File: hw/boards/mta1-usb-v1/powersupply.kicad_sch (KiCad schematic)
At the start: 19 parts, among them U1 MCP1824T-2502EOT, U2 MIC5258-1.2YM5, U9 NCP752BSN33T1G

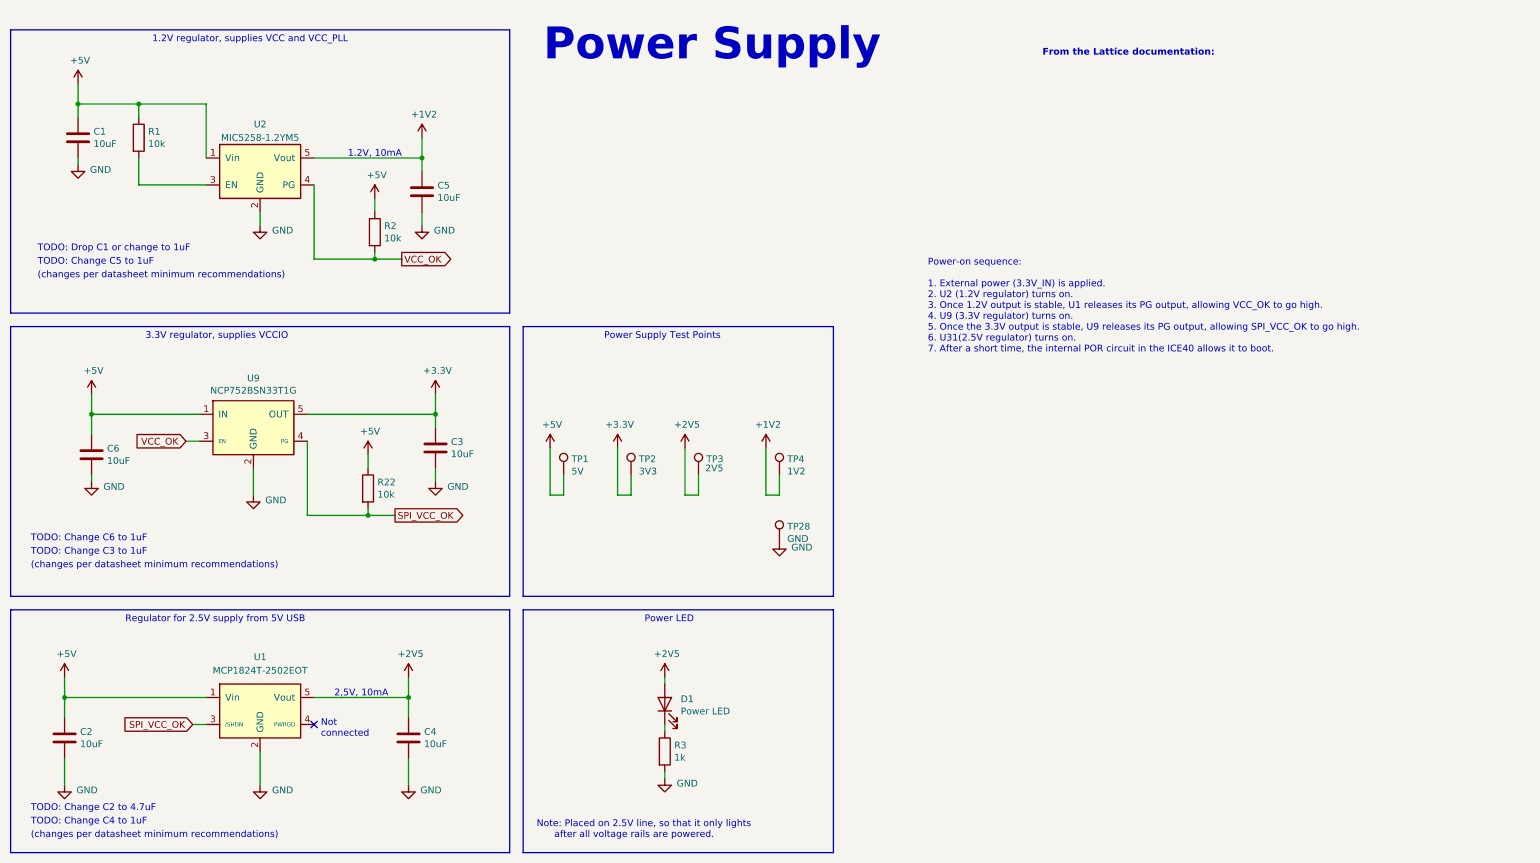
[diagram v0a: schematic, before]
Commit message: Add extended values, manufacturer/distributor info to components in mta1
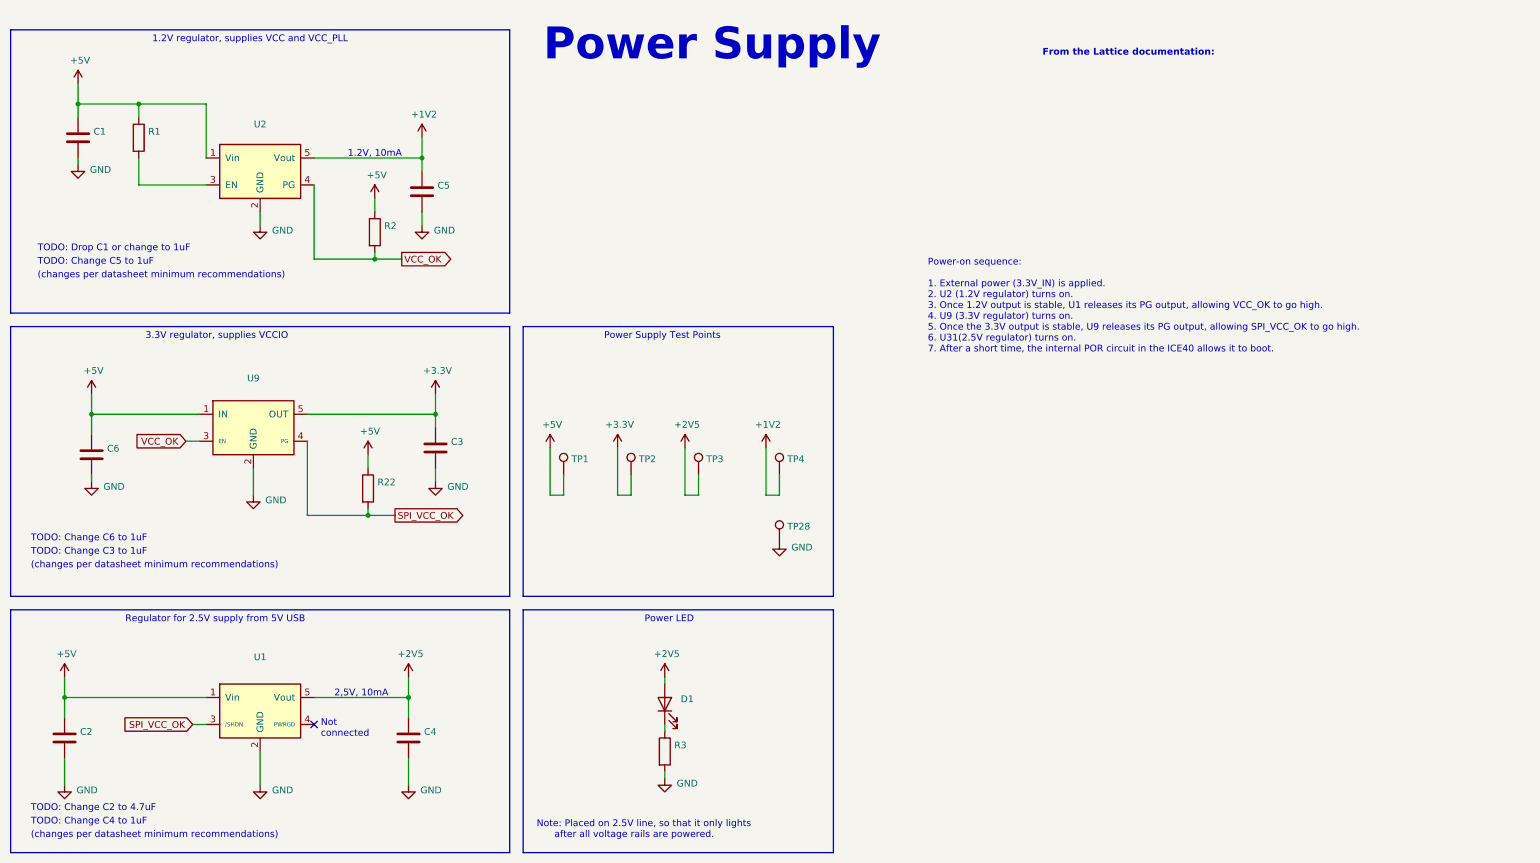
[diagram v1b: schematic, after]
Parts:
- C1, C2, C3, C4, C5, C6: value 10uF -> (none); footprint mta1:CAPC1608X09L -> (none); Extended Value (none) -> 10V,X5R,20%; Manufacturer (none) -> Any/not critical
- D1: value Power LED -> (none); footprint LED_SMD:LED_0402_1005Metric -> (none); Manufacturer (none) -> Foshan NationStar; Manufacturer Part Number (none) -> NCD0402B1; Supplier (none) -> LCSC; Supplier Part Number (none) -> C130724
- R1, R2, R22: value 10k -> (none); footprint mta1:ERJ2G(0402)_L -> (none); Extended Value (none) -> 1/16W,5%; Manufacturer (none) -> Any/not critical
- R3: value 1k -> (none); footprint mta1:ERJ2G(0402)_L -> (none); Extended Value (none) -> 1/16W,5%; Manufacturer (none) -> Any/not critical
- TP1: value 5V -> (none); footprint TestPoint:TestPoint_Pad_D1.0mm -> (none); now left out of the parts list
- TP2: value 3V3 -> (none); footprint TestPoint:TestPoint_Pad_D1.0mm -> (none); now left out of the parts list
- TP28: value GND -> (none); footprint TestPoint:TestPoint_Pad_D1.0mm -> (none); now left out of the parts list
- TP3: value 2V5 -> (none); footprint TestPoint:TestPoint_Pad_D1.0mm -> (none); now left out of the parts list
- TP4: value 1V2 -> (none); footprint TestPoint:TestPoint_Pad_D1.0mm -> (none); now left out of the parts list
- U1: value MCP1824T-2502EOT -> (none); footprint Package_TO_SOT_SMD:SOT-23-5 -> (none); symbol mta1:MCP1824 -> mta1:MCP1824T-2502EOT; Manufacturer (none) -> Microchip; Manufacturer Part Number (none) -> MCP1824T-2502EOT; Supplier (none) -> Digikey; Supplier Part Number (none) -> MCP1824T-2502E/OTCT-ND
- U2: value MIC5258-1.2YM5 -> (none); footprint Package_TO_SOT_SMD:SOT-23-5 -> (none); Manufacturer (none) -> Micrel Inc.; Manufacturer Part Number (none) -> MIC5258-1.2YM5; Supplier (none) -> Digikey; Supplier Part Number (none) -> 2156-MIC5258-1.2YM5-ND
- U9: value NCP752BSN33T1G -> (none); footprint mta1:NCP752BSN33T1G -> (none); Manufacturer (none) -> onsemi; Manufacturer Part Number (none) -> NCP752BSN33T1G; Supplier (none) -> Digikey; Supplier Part Number (none) -> NCP752BSN33T1GOSCT-ND
